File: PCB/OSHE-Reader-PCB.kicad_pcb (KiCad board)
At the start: 4 copper layers, 118.5 x 160.4 mm, 73 parts, among them J1 USB_C_Receptacle_PowerOnly_24P, J2 112L-TDA0, J3 Conn_01x24_MountingPin, Q1 PNP, Q2 Si1308EDL, SW1 SW_Push, SW2 SW_Push, SW3 SW_Push, SW4 SW_Push, SW5 SW_Push, U1 BQ2057CSNTR, U2 IRF7326D2TRPBF, U3 TPS5432DDA

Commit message: Did a bunch of work with final preparations of the schematic for pcb routing
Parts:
- added H1: MountingHole, MountingHole:MountingHole_3.2mm_M3, F.Cu at (-21.5, 112.5)
- added H2: MountingHole, MountingHole:MountingHole_3.2mm_M3, F.Cu at (-21.5, 120.4)
- added H3: MountingHole, MountingHole:MountingHole_3.2mm_M3, F.Cu at (-21.5, 128.4)
- added H4: MountingHole, MountingHole:MountingHole_3.2mm_M3, F.Cu at (-21.5, 136.3)
- added J4: S2B-PH-K-SLFSN, S2B_PH_K_S_LF__SN_:CONN_S2B-PH-K-S_JST, F.Cu at (-5.51, 73.0)
- added LED1: HSMY-C110, ul_HSMY-C110:LED3_HSMx-C110_AVA, F.Cu at (0.94, 49.3)
- added R1: 5.1k, Resistor_SMD:R_1206_3216Metric, F.Cu at (-1.20, 33.6)
- added R2: 5.1k, Resistor_SMD:R_1206_3216Metric, F.Cu at (-1.20, 36.9)
- added R3: R_{T2}/6.8K, Resistor_SMD:R_1206_3216Metric, F.Cu at (-74.2, 83.8)
- J1: value USB_C_Receptacle_PowerOnly_24P -> 2171750001; footprint USB4125_GF_A:CONN6_USB4125_GCT -> 2171750001:2171750001_MOL
- moved J1 31.2 mm to (1.70, 27.6)
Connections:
- R23 pad 2: Net-(D4-A) -> Net-(LED1-Pad3)

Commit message: Added edge cuts with proper sizing for case, and properly positioned mounting holes for case, started positioning larger components
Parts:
- moved SW1 218.2 mm to (149.0, 40.0), turned to 90 degrees
- moved SW2 215.7 mm to (149.0, 51.2), turned to 90 degrees
- moved U4 205.6 mm to (125.2, 82.8), turned to 90 degrees
- moved J3 163.7 mm to (110.5, 30.4)
- moved H2 161.1 mm to (138.8, 104.5)
- moved SW5 152.1 mm to (97.5, 112.5)
- moved SW3 139.0 mm to (47.0, 41.0), turned to -90 degrees
- moved SW4 135.4 mm to (47.0, 51.2), turned to -90 degrees
- moved J1 133.8 mm to (97.5, 121.0)
- moved U2 122.8 mm to (61.0, 115.2)
- moved U3 122.8 mm to (71.5, 115.2)
- moved J2 113.9 mm to (49.3, 83.6), turned to -90 degrees
- moved U1 111.0 mm to (51.1, 116.2)
- moved J4 92.4 mm to (78.0, 33.5), turned to 180 degrees
- moved H1 78.2 mm to (56.2, 104.5)
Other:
- board size 118.5 x 160.4 mm -> 115 x 100 mm

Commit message: PCB Update
updated PCB with dimensions and took notes on said dimensions based on case CAD model
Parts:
- moved U4 212.2 mm to (-67.5, -6.00)
- moved J1 196.4 mm to (-93.7, 76.0)
- moved SW5 196.4 mm to (-93.7, 67.5)
- moved J3 186.0 mm to (-75.5, 31.5)
- moved H3 180.9 mm to (130.5, 30.3)
- moved H2 171.8 mm to (-30.0, 136.5)
- moved U1 170.3 mm to (-88.3, 18.3)
- moved U2 170.3 mm to (-78.4, 17.4)
- moved U3 170.3 mm to (-67.9, 17.3)
- moved SW1 165.0 mm to (-12.5, 6.25)
- moved SW2 165.0 mm to (-12.5, 17.5)
- moved SW3 136.5 mm to (-89.5, 37.8)
- moved SW4 136.5 mm to (-89.5, 48.0)
- moved J2 130.3 mm to (-75.7, 46.9)
- moved J4 104.5 mm to (-23.1, 7.02)
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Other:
- board size 115 x 100 mm -> 118.5 x 160.4 mm

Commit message: shortened pcb to make room for battery and started laying out components
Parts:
- moved U4 212.2 mm to (125.2, 82.8)
- moved J1 196.4 mm to (97.5, 121.0)
- moved SW5 196.4 mm to (97.5, 112.5)
- moved J3 186.0 mm to (110.5, 30.4)
- moved H3 180.9 mm to (-21.5, 128.4)
- moved H2 171.8 mm to (138.8, 104.5)
- moved U1 170.3 mm to (51.1, 116.2)
- moved U2 170.3 mm to (61.0, 115.2)
- moved U3 170.3 mm to (71.5, 115.2)
- moved SW1 165.0 mm to (149.0, 40.0)
- moved SW2 165.0 mm to (149.0, 51.2)
- moved SW3 136.5 mm to (47.0, 41.0)
- moved SW4 136.5 mm to (47.0, 51.2)
- moved J2 130.3 mm to (49.3, 83.6)
- moved J4 104.5 mm to (78.0, 33.5)
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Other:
- board size 118.5 x 160.4 mm -> 115 x 100 mm

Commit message: Definative PCB edge cuts
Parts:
- J1, J2, J3, J4, U1, U2, U3, U4: moved to B.Cu
- moved LED1 112.5 mm to (85.7, 123.4), turned to -90 degrees
- moved J2 81.5 mm to (124.3, 115.6), turned to 180 degrees
- moved J3 74.4 mm to (46.5, 68.4), turned to -90 degrees
- turned J1 to 180 degrees
- turned J4 to 0 degrees
- turned U1 to 180 degrees
- turned U2 to 180 degrees
- turned U3 to 180 degrees
- turned U4 to -90 degrees
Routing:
- added copper zone on In2.Cu, net +3V3
- added copper zone on In1.Cu, net GND

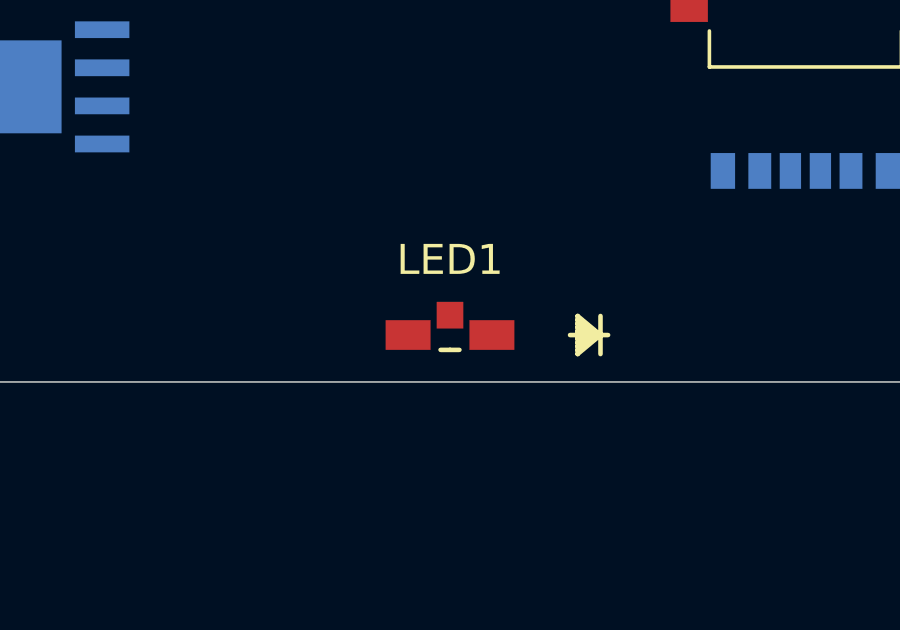
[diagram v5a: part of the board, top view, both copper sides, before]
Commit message: Fixed some items being connected to +3V3 and some to +3.3V
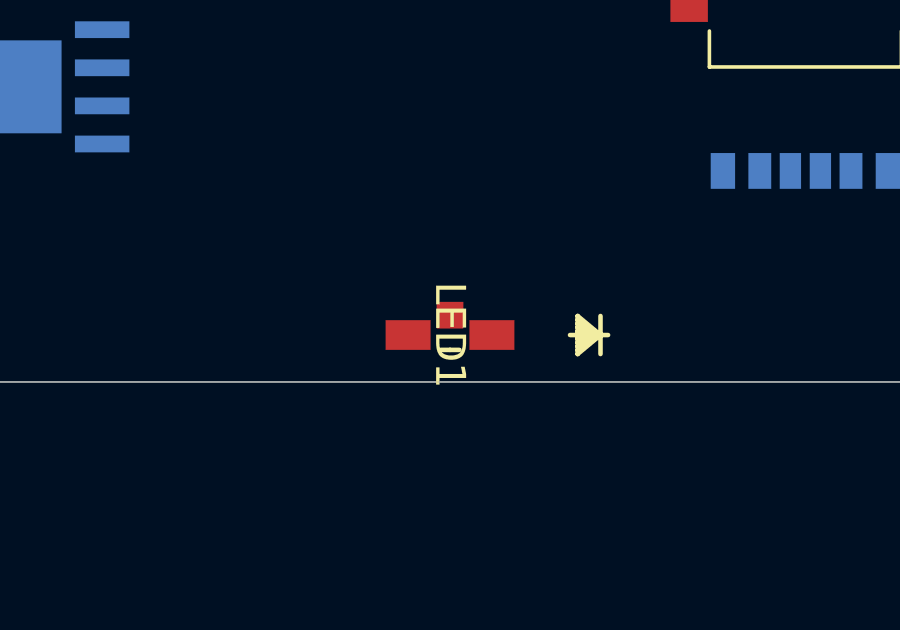
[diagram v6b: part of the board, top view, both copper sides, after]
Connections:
- C10 pad 2: +3.3V -> +3V3
- C11 pad 2: +3.3V -> +3V3
- L1 pad 2: +3.3V -> +3V3
- R11 pad 1: +3.3V -> +3V3
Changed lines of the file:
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@@
 	(net 78 "Net-(C8-Pad2)")
 	(net 79 "Net-(C9-Pad2)")
-	(net 80 "+3.3V")
-	(net 81 "Net-(D4-A)")
-	(net 82 "Net-(Q1-B)")
-	(net 83 "Net-(LED1-Pad3)")
-	(net 84 "unconnected-(LED1-Pad2)")
+	(net 80 "Net-(D4-A)")
+	(net 81 "Net-(Q1-B)")
+	(net 82 "Net-(LED1-Pad3)")
+	(net 83 "unconnected-(LED1-Pad2)")
 	(footprint "Resistor_SMD:R_1206_3216Metric"
 		(layer "F.Cu")
@@
 			(layers "F.Cu" "F.Mask" "F.Paste")
 			(roundrect_rratio 0.217391)
-			(net 80 "+3.3V")
+			(net 23 "+3V3")
 			(pintype "passive")
 		)
@@
 			(layers "F.Cu" "F.Mask" "F.Paste")
 			(roundrect_rratio 0.222222)
-			(net 83 "Net-(LED1-Pad3)")
+			(net 82 "Net-(LED1-Pad3)")
 			(pintype "passive")
 		)
@@
 			(layers "F.Cu" "F.Mask" "F.Paste")
 			(roundrect_rratio 0.2)
-			(net 81 "Net-(D4-A)")
+			(net 80 "Net-(D4-A)")
 			(pinfunction "A")
 			(pintype "passive")
@@
 			(layers "F.Cu" "F.Mask" "F.Paste")
 			(roundrect_rratio 0.238095)
-			(net 80 "+3.3V")
+			(net 23 "+3V3")
 			(pinfunction "2")
 			(pintype "passive")
@@
 			(layers "F.Cu" "F.Mask" "F.Paste")
 			(roundrect_rratio 0.222222)
-			(net 80 "+3.3V")
+			(net 23 "+3V3")
 			(pintype "passive")
 		)
@@
 			(layers "*.Cu" "*.Mask")
 			(remove_unused_layers no)
-			(net 82 "Net-(Q1-B)")
+			(net 81 "Net-(Q1-B)")
 			(pinfunction "B")
 			(pintype "input")
@@
 			(layers "F.Cu" "F.Mask" "F.Paste")
 			(roundrect_rratio 0.222222)
-			(net 82 "Net-(Q1-B)")
+			(net 81 "Net-(Q1-B)")
 			(pintype "passive")
 		)
@@
 			(layers "F.Cu" "F.Mask" "F.Paste")
 			(roundrect_rratio 0.217391)
-			(net 80 "+3.3V")
+			(net 23 "+3V3")
 			(pintype "passive")
 		)
@@
 		(tags "HSMY-C110 ")
 		(property "Reference" "LED1"
-			(at -2.5 0 0)
+			(at 0 0 270)
 			(unlocked yes)
 			(layer "F.SilkS")
@@
 		)
 		(property "Value" "HSMY-C110"
-			(at 0 0 0)
+			(at 0 0 270)
 			(unlocked yes)
 			(layer "F.Fab")
@@
 		)
 		(property "Datasheet" "HSMY-C110"
-			(at 0 0 90)
+			(at 0 0 270)
 			(layer "F.Fab")
 			(hide yes)
@@
 		)
 		(property "Description" ""
-			(at 0 0 90)
+			(at 0 0 270)
 			(layer "F.Fab")
 			(hide yes)
@@
 		)
 		(fp_text user "${REFERENCE}"
-			(at 0 0 0)
+			(at 0 0 270)
 			(unlocked yes)
 			(layer "F.Fab")
@@
 			(size 0.889 0.889)
 			(layers "F.Cu" "F.Mask" "F.Paste")
-			(net 84 "unconnected-(LED1-Pad2)")
+			(net 83 "unconnected-(LED1-Pad2)")
 			(pintype "unspecified+no_connect")
 		)
@@
 			(size 0.9906 1.4986)
 			(layers "F.Cu" "F.Mask" "F.Paste")
-			(net 83 "Net-(LED1-Pad3)")
+			(net 82 "Net-(LED1-Pad3)")
 			(pintype "unspecified")
 		)
@@
 		(fp_text user "*"
 			(at -0.508 4.064 0)
+			(unlocked yes)
 			(layer "B.SilkS")
 			(effects
@@
 		(fp_text user "*"
 			(at -0.508 4.064 0)
-			(unlocked yes)
 			(layer "B.SilkS")
 			(effects
@@
 			)
 		)
-		(fp_text user "*"
-			(at -0.508 2.286 0)
+		(fp_text user "${REFERENCE}"
+			(at 0 3.0344 0)
 			(unlocked yes)
 			(layer "B.Fab")
@@
 			)
 		)
-		(fp_text user "${REFERENCE}"
-			(at 0 3.0344 0)
+		(fp_text user "*"
+			(at -0.508 2.286 0)
 			(unlocked yes)
 			(layer "B.Fab")
@@
 		)
 		(embedded_fonts no)
-		(model "${KICAD9_3DMODEL_DIR}/Connector_USB.3dshapes/USB_C_Receptacle_Amphenol_12401610E4-2A.step"
-			(offset
-				(xyz 0 0 0)
-			)
-			(scale
-				(xyz 1 1 1)
-			)
-			(rotate
-				(xyz 0 0 0)
-			)
-		)
-		(model "${KICAD9_3DMODEL_DIR}/Connector_USB.3dshapes/USB_C_Receptacle_GCT_USB4125-xx-x_6P_TopMnt_Horizontal.step"
-			(offset
-				(xyz 0 0 0)
-			)
-			(scale
-				(xyz 1 1 1)
-			)
-			(rotate
-				(xyz 0 0 0)
-			)
-		)
-		(model "${KICAD9_3DMODEL_DIR}/Connector_USB.3dshapes/USB_C_Receptacle_GCT_USB4125-xx-x-0190_6P_TopMnt_Horizontal.step"
-			(offset
-				(xyz 0 0 0)
-			)
-			(scale
-				(xyz 1 1 1)
-			)
-			(rotate
-				(xyz 0 0 0)
-			)
-		)
 	)
 	(footprint "BQ2057CSNTR:D8"
